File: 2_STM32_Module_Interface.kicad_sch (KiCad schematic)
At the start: 14 parts, among them U3 WeAct STM32F405RG

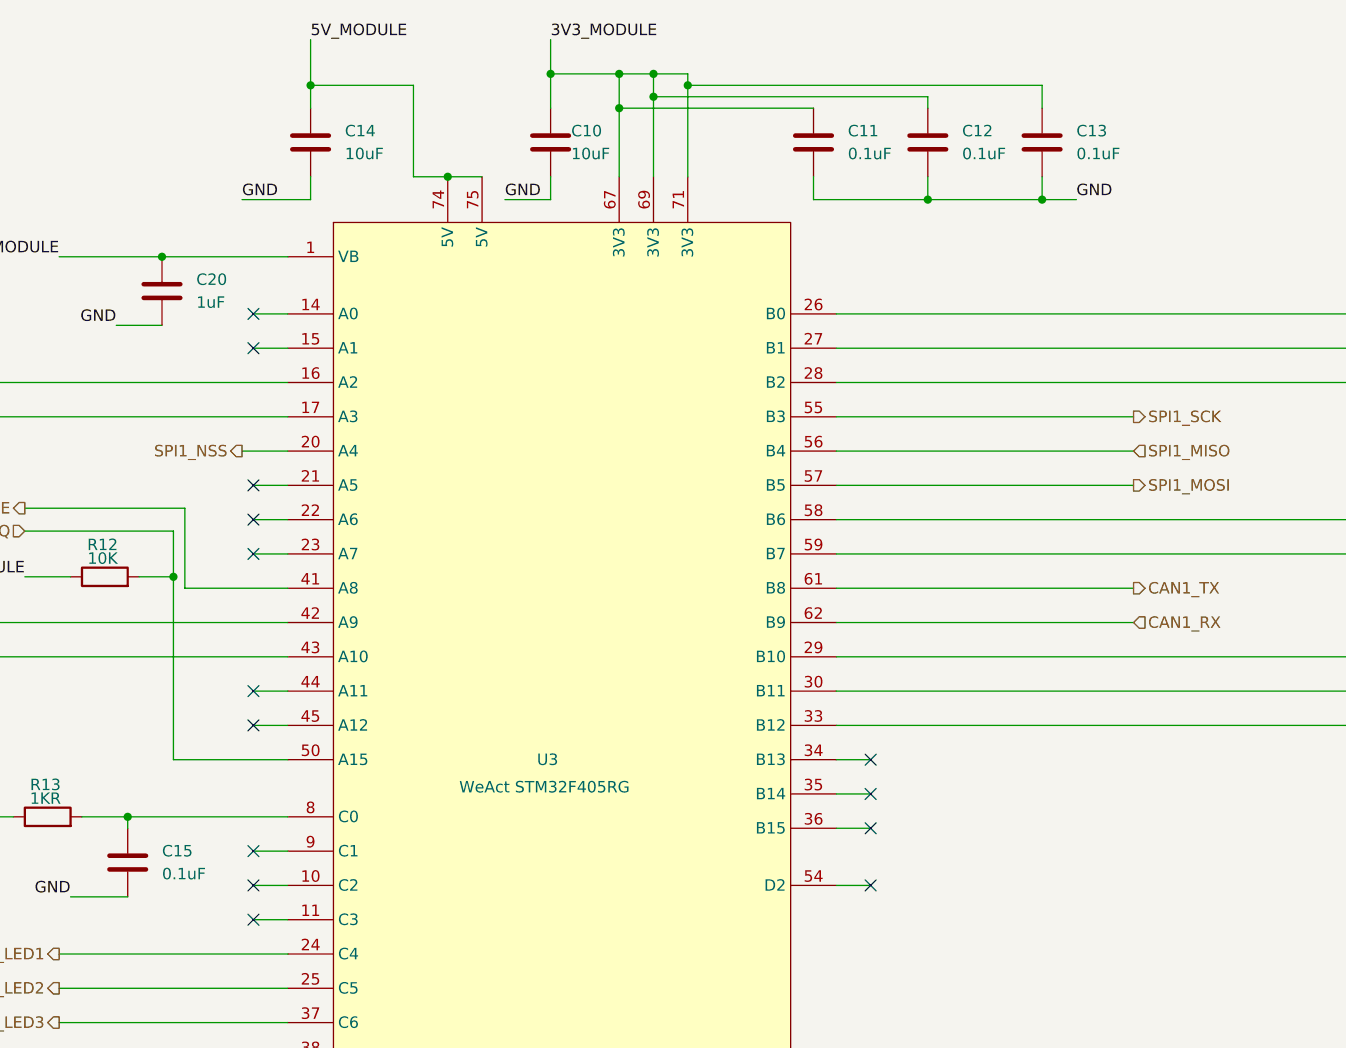
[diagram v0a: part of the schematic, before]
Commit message: Updated BOM. Initial review and corrections
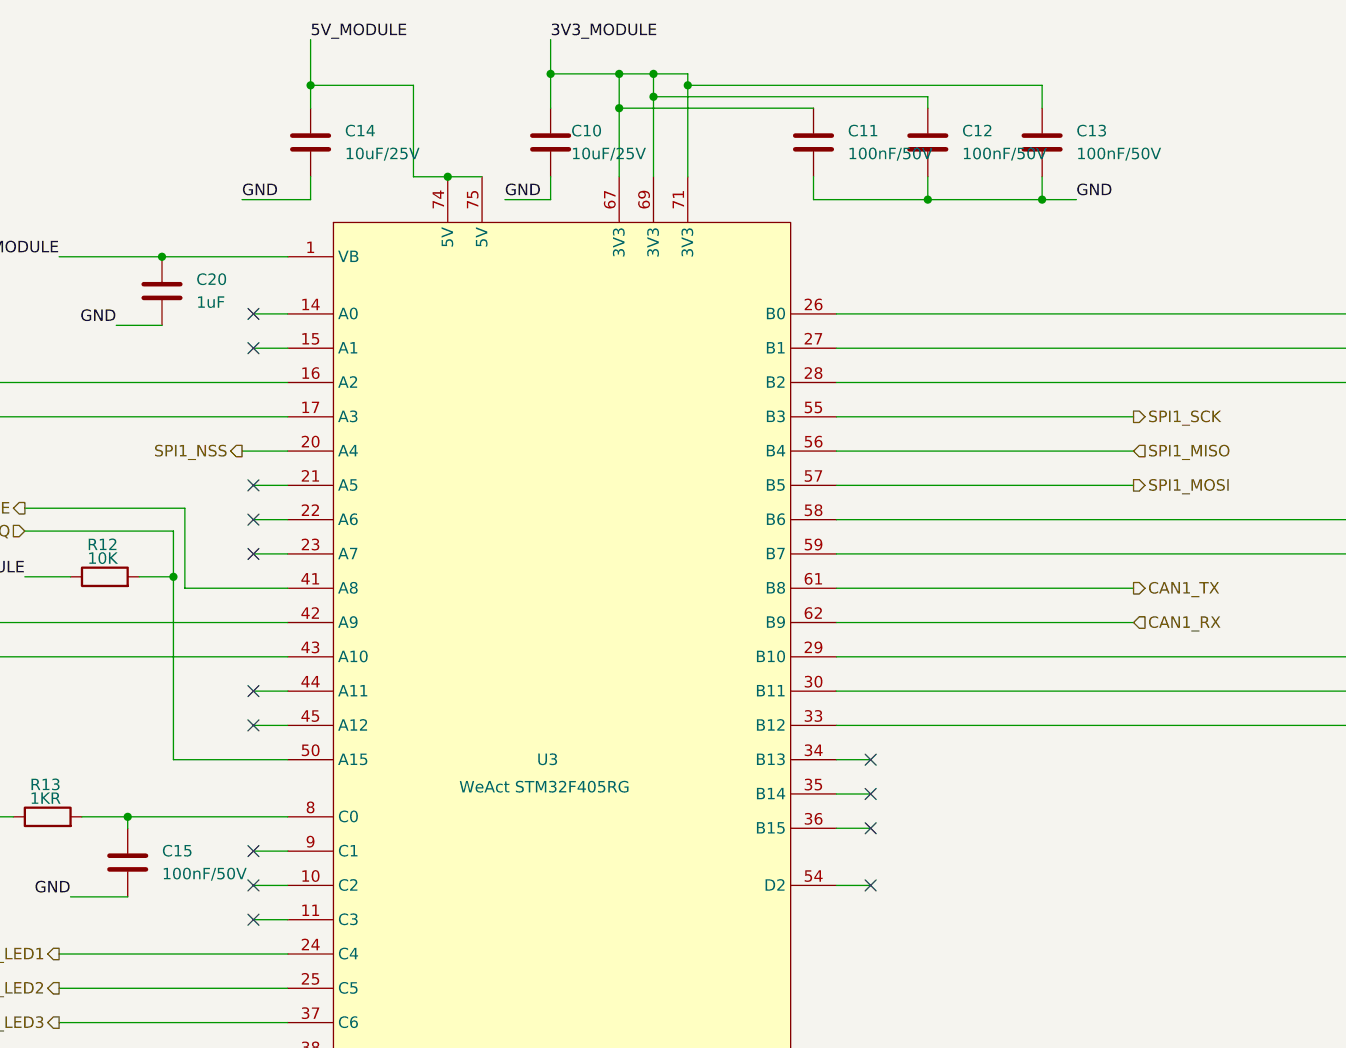
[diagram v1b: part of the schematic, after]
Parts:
- C10, C14: value 10uF -> 10uF/25V; LCSC C13585 -> C6119815
- C11, C12, C13, C15: value 0.1uF -> 100nF/50V; LCSC C1848 -> C6119867
- C20: LCSC C1848 -> C5199872
- FB20, FB21: LCSC C1015 -> C16902
- R12: LCSC C17902 -> C15401
- R13: LCSC C17909 -> C14676
- U3: now left out of the parts list

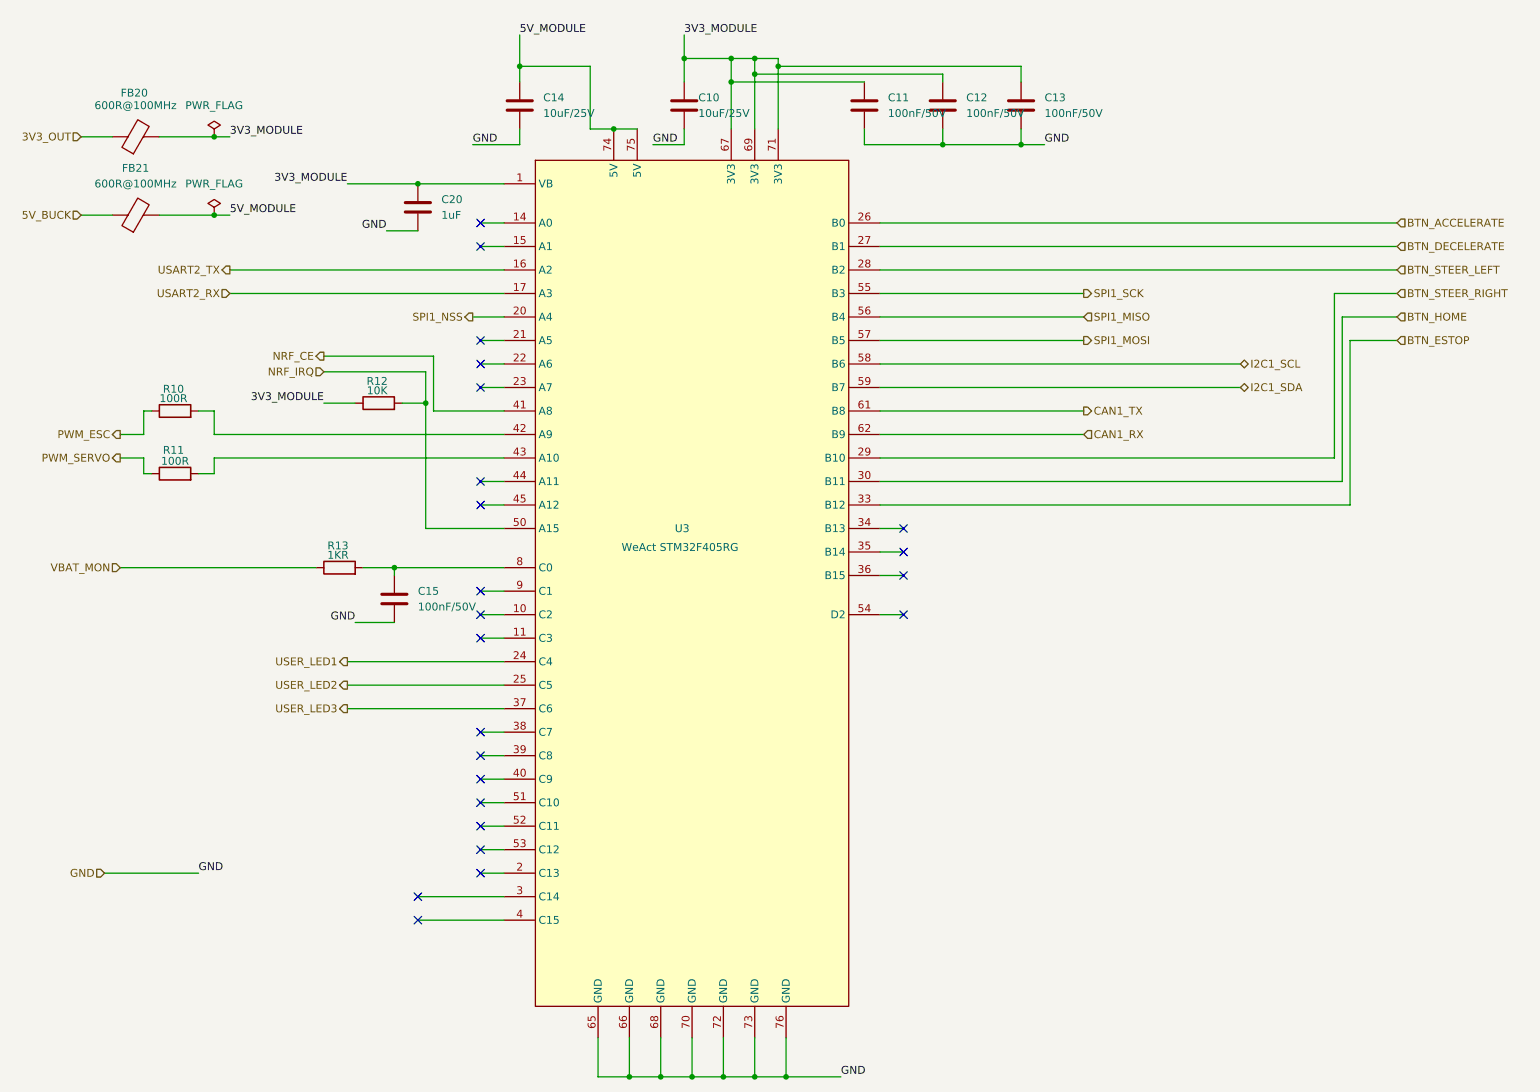
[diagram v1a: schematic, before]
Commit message: Cleaned up schematic. Added mounting holes.
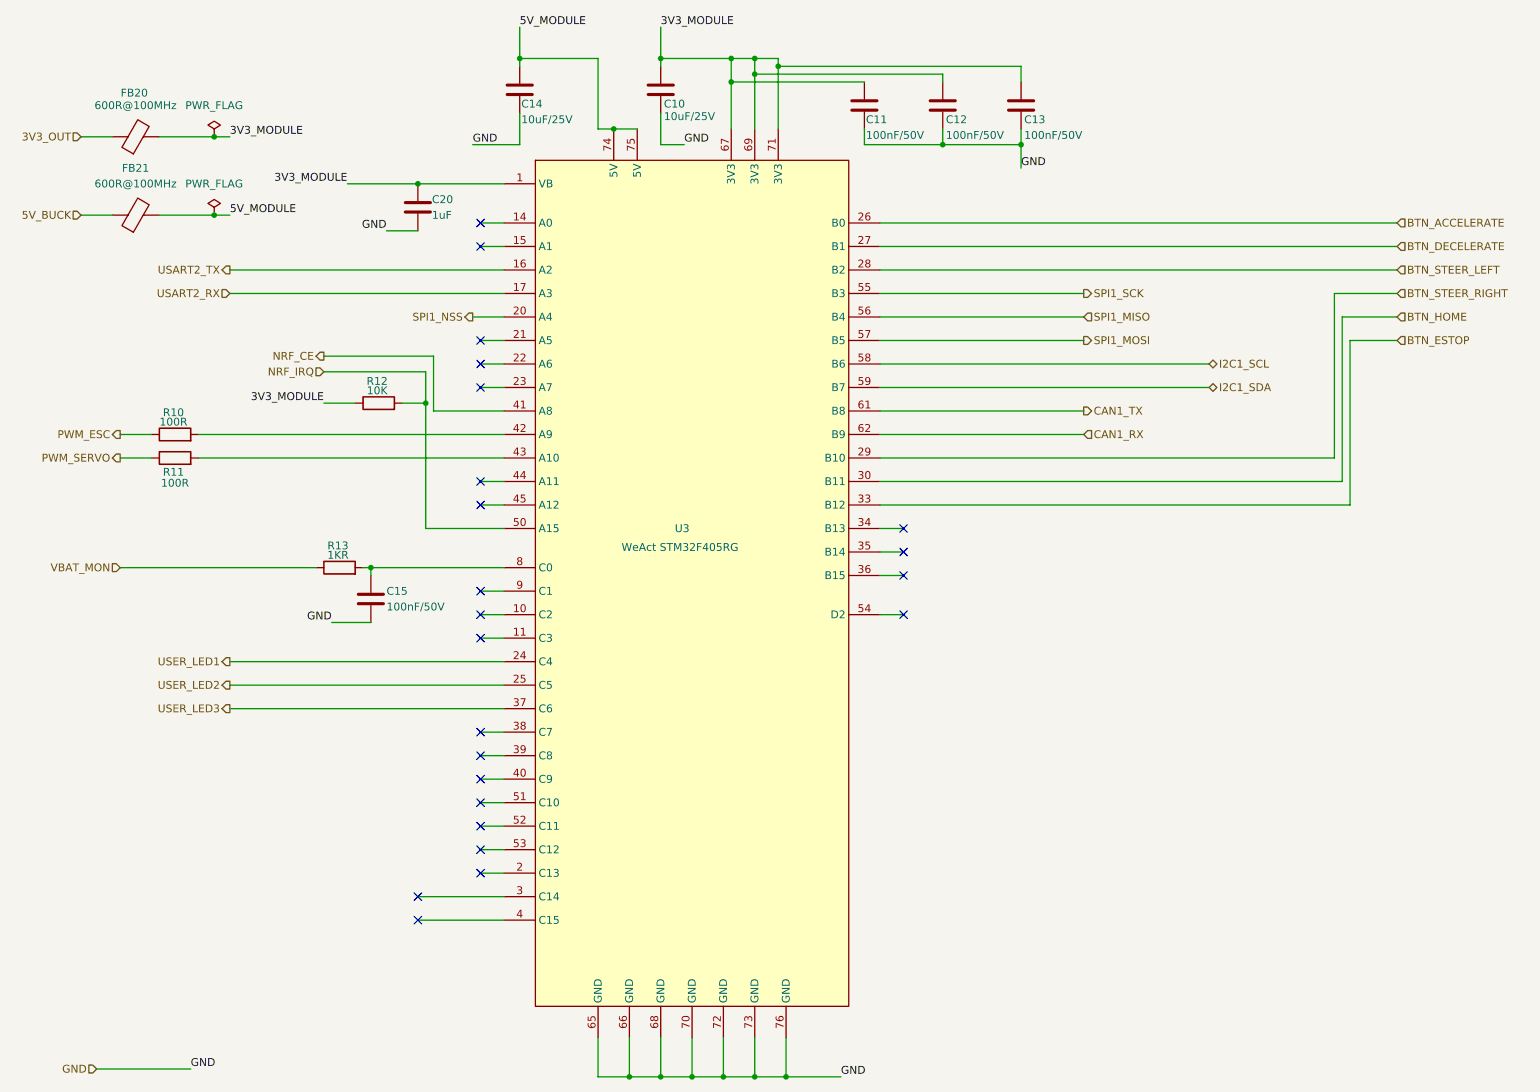
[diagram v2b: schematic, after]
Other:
- moved on the sheet: C10, C14, C15, R10, R11
